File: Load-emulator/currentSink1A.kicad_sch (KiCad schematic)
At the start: 3 parts, among them Q2 TIP41C, U2 AD8001AN

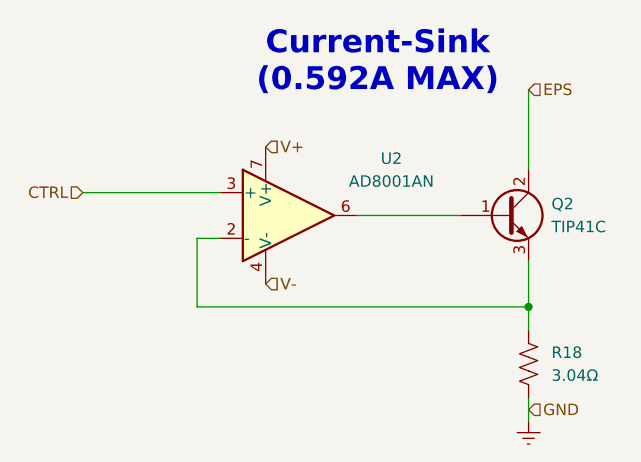
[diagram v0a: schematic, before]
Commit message: Replacement of the microcontroller w/ picoblade
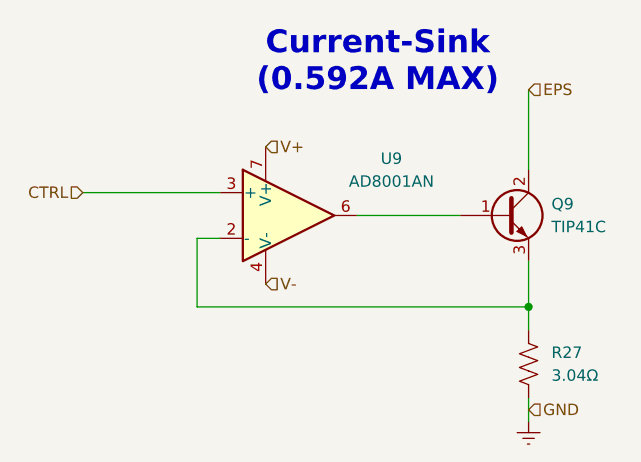
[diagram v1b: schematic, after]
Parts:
- renumbered Q2 to Q9, R18 to R27, U2 to U9
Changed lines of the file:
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@@
 		(dnp no)
 		(fields_autoplaced yes)
-		(property "Reference" "#PWR025"
+		(property "Reference" "#PWR060"
 			(at 162.56 114.3 0)
 			(effects
@@
 		(dnp no)
 		(fields_autoplaced yes)
-		(property "Reference" "Q2"
+		(property "Reference" "Q9"
 			(at 165.1 83.8199 0)
 			(effects
@@
 		(dnp no)
 		(fields_autoplaced yes)
-		(property "Reference" "U2"
+		(property "Reference" "U9"
 			(at 147.32 78.7714 0)
 			(effects
@@
 		(dnp no)
 		(fields_autoplaced yes)
-		(property "Reference" "R18"
+		(property "Reference" "R27"
 			(at 165.1 100.3299 0)
 			(effects

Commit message: Added footprints for the remaining resistors, capacitors and ampops, as well as some 3D models
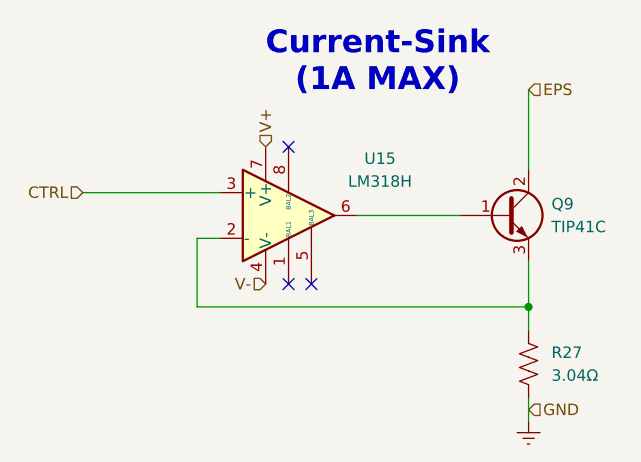
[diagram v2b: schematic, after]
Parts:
- removed U9: AD8001AN, Package_DIP:DIP-8_W7.62mm, symbol Amplifier_Operational:AD8001AN
- added U15: LM318H, symbol Amplifier_Operational:LM318H
- R27: footprint (none) -> Resistor_SMD:R_0201_0603Metric
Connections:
- net CTRL: now also U15.3 (+)
- net V+: now also U15.7 (V+)
- net V-: now also U15.4 (V-)
- net at Q9.1 (B): now also U15.6
- net at Q9.3 (E), R27.1: now also U15.2 (-)
- no-connect marks 0 -> 3
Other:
- note added: "Current-Sink (1A MAX)"
- note removed: "Current-Sink (0.592A MAX)"
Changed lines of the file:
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@@
 		(color 0 0 0 0)
 	)
+	(no_connect
+		(at 138.43 92.71)
+	)
+	(no_connect
+		(at 135.89 92.71)
+	)
+	(no_connect
+		(at 135.89 77.47)
+	)
 	(wire
 		(pts
@@
 		)
 	)
-	(text "Current-Sink\n(0.592A MAX)\n"
+	(text "Current-Sink\n(1A MAX)\n"
 		(exclude_from_sim no)
 		(at 145.796 68.072 0)
@@
 	(hierarchical_label "V-"
 		(shape input)
-		(at 133.35 92.71 0)
+		(at 133.35 92.71 180)
 		(fields_autoplaced yes)
 		(effects
@@
 				(size 1.27 1.27)
 			)
-			(justify left)
+			(justify right)
 		)
 	)
 	(hierarchical_label "V+"
 		(shape input)
-		(at 133.35 77.47 0)
+		(at 133.35 77.47 90)
 		(fields_autoplaced yes)
 		(effects
@@
 	)
 	(symbol
+		(lib_id "Amplifier_Operational:LM318H")
+		(at 135.89 85.09 0)
+		(unit 1)
+		(exclude_from_sim no)
+		(in_bom yes)
+		(on_board yes)
+		(dnp no)
+		(fields_autoplaced yes)
+		(property "Reference" "U15"
+			(at 146.05 78.7714 0)
+			(effects
+				(font
+					(size 1.27 1.27)
+				)
+			)
+		)
+		(property "Value" "LM318H"
+			(at 146.05 81.3114 0)
+			(effects
+				(font
+					(size 1.27 1.27)
+				)
+			)
+		)
+		(property "Footprint" ""
+			(at 135.89 85.09 0)
+			(effects
+				(font
+					(size 1.27 1.27)
+				)
+				(hide yes)
+			)
+		)
+		(property "Datasheet" "http://www.ti.com/lit/ds/symlink/lm318-n.pdf"
+			(at 135.89 85.09 0)
+			(effects
+				(font
+					(size 1.27 1.27)
+				)
+				(hide yes)
+			)
+		)
+		(property "Description" "Operational Amplifier, TO-99-8"
+			(at 135.89 85.09 0)
+			(effects
+				(font
+					(size 1.27 1.27)
+				)
+				(hide yes)
+			)
+		)
+		(pin "6"
+		)
+		(pin "5"
+		)
+		(pin "1"
+		)
+		(pin "4"
+		)
+		(pin "3"
+		)
+		(pin "2"
+		)
+		(pin "8"
+		)
+		(pin "7"
+		)
+		(instances
+			(project ""
+				(path "/9054bfd2-3cc0-4c96-aa71-abdb09b76dc7/a12c045f-372a-4c5b-93d1-0c234b5f9c5c/00308429-beaf-4782-9e5d-10502f61f5c3"
+					(reference "U17")
+					(unit 1)
+				)
+				(path "/9054bfd2-3cc0-4c96-aa71-abdb09b76dc7/a12c045f-372a-4c5b-93d1-0c234b5f9c5c/1067bc1d-731b-4056-a052-e9f9516161f7"
+					(reference "U15")
+					(unit 1)
+				)
+				(path "/9054bfd2-3cc0-4c96-aa71-abdb09b76dc7/a12c045f-372a-4c5b-93d1-0c234b5f9c5c/205d1fd4-c06c-4b81-92b9-38f15798e8a4"
+					(reference "U14")
+					(unit 1)
+				)
+				(path "/9054bfd2-3cc0-4c96-aa71-abdb09b76dc7/a12c045f-372a-4c5b-93d1-0c234b5f9c5c/7c366463-52c3-40cf-bddf-8ecdc0d5aa81"
+					(reference "U18")
+					(unit 1)
+				)
+				(path "/9054bfd2-3cc0-4c96-aa71-abdb09b76dc7/a12c045f-372a-4c5b-93d1-0c234b5f9c5c/9489fc74-437b-459f-aea1-db601c07bed5"
+					(reference "U16")
+					(unit 1)
+				)
+			)
+		)
+	)
+	(symbol
 		(lib_id "Transistor_BJT:TIP41C")
 		(at 160.02 85.09 0)
@@
 				(path "/9054bfd2-3cc0-4c96-aa71-abdb09b76dc7/a12c045f-372a-4c5b-93d1-0c234b5f9c5c/9489fc74-437b-459f-aea1-db601c07bed5"
 					(reference "Q6")
-					(unit 1)
-				)
-			)
-		)
-	)
-	(symbol
-		(lib_id "Amplifier_Operational:AD8001AN")
-		(at 135.89 85.09 0)
-		(unit 1)
-		(exclude_from_sim no)
-		(in_bom yes)
-		(on_board yes)
-		(dnp no)
-		(fields_autoplaced yes)
-		(property "Reference" "U9"
-			(at 147.32 78.7714 0)
-			(effects
-				(font
-					(size 1.27 1.27)
-				)
-			)
-		)
-		(property "Value" "AD8001AN"
-			(at 147.32 81.3114 0)
-			(effects
-				(font
-					(size 1.27 1.27)
-				)
-			)
-		)
-		(property "Footprint" "Package_DIP:DIP-8_W7.62mm"
-			(at 133.35 90.17 0)
-			(effects
-				(font
-					(size 1.27 1.27)
-				)
-				(justify left)
-				(hide yes)
-			)
-		)
-		(property "Datasheet" "https://www.analog.com/media/en/technical-documentation/data-sheets/ad8001.pdf"
-			(at 139.7 81.28 0)
-			(effects
-				(font
-					(size 1.27 1.27)
-				)
-				(hide yes)
-			)
-		)
-		(property "Description" "Current Feedback Amplifier, 800 MHz, 50mW, DIP-8"
-			(at 135.89 85.09 0)
-			(effects
-				(font
-					(size 1.27 1.27)
-				)
-				(hide yes)
-			)
-		)
-		(pin "6"
-		)
-		(pin "1"
-		)
-		(pin "3"
-		)
-		(pin "8"
-		)
-		(pin "5"
-		)
-		(pin "4"
-		)
-		(pin "7"
-		)
-		(pin "2"
-		)
-		(instances
-			(project "Load-emulator"
-				(path "/9054bfd2-3cc0-4c96-aa71-abdb09b76dc7/a12c045f-372a-4c5b-93d1-0c234b5f9c5c/00308429-beaf-4782-9e5d-10502f61f5c3"
-					(reference "U9")
-					(unit 1)
-				)
-				(path "/9054bfd2-3cc0-4c96-aa71-abdb09b76dc7/a12c045f-372a-4c5b-93d1-0c234b5f9c5c/1067bc1d-731b-4056-a052-e9f9516161f7"
-					(reference "U3")
-					(unit 1)
-				)
-				(path "/9054bfd2-3cc0-4c96-aa71-abdb09b76dc7/a12c045f-372a-4c5b-93d1-0c234b5f9c5c/205d1fd4-c06c-4b81-92b9-38f15798e8a4"
-					(reference "U2")
-					(unit 1)
-				)
-				(path "/9054bfd2-3cc0-4c96-aa71-abdb09b76dc7/a12c045f-372a-4c5b-93d1-0c234b5f9c5c/7c366463-52c3-40cf-bddf-8ecdc0d5aa81"
-					(reference "U12")
-					(unit 1)
-				)
-				(path "/9054bfd2-3cc0-4c96-aa71-abdb09b76dc7/a12c045f-372a-4c5b-93d1-0c234b5f9c5c/9489fc74-437b-459f-aea1-db601c07bed5"
-					(reference "U6")
 					(unit 1)
 				)
@@
 			)
 		)
-		(property "Footprint" ""
+		(property "Footprint" "Resistor_SMD:R_0201_0603Metric"
 			(at 163.576 101.854 90)
 			(effects

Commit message: Forgot to save files before last commit
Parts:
- U15: footprint (none) -> LM318M:SOIC127P599X175-8N
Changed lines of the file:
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@@
 			)
 		)
-		(property "Footprint" ""
+		(property "Footprint" "LM318M:SOIC127P599X175-8N"
 			(at 135.89 85.09 0)
 			(effects

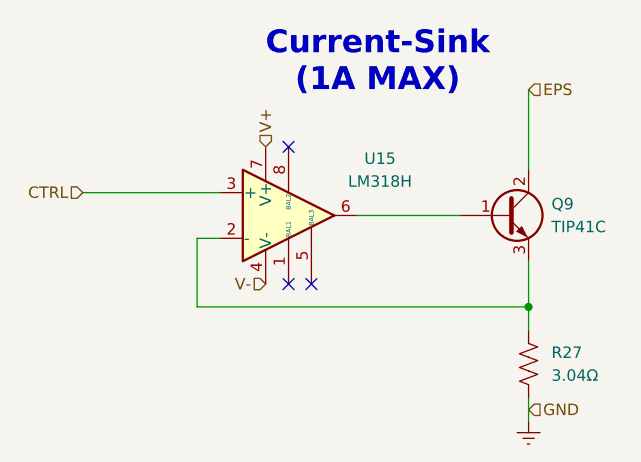
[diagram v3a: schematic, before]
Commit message: File with 3D models were created, because the models were previously saved at a local PC, so only one specific machine could load them; Better organization; EPS terminal labels were added to each current sink channel; Channels were searched for possible errors
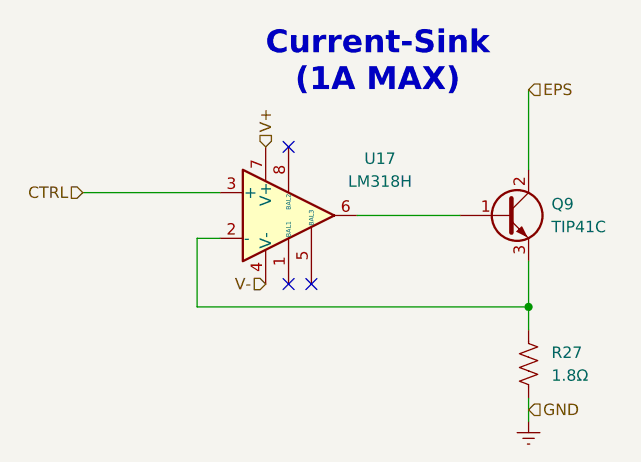
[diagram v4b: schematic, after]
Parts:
- R27: value 3.04Ω -> 1.8Ω
- renumbered U15 to U17
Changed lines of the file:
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@@
 		(dnp no)
 		(fields_autoplaced yes)
-		(property "Reference" "U15"
+		(property "Reference" "U17"
 			(at 146.05 78.7714 0)
 			(effects
@@
 			)
 		)
-		(property "Value" "3.04Ω"
+		(property "Value" "1.8Ω"
 			(at 165.1 102.8699 0)
 			(effects

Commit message: minor changes in connectors
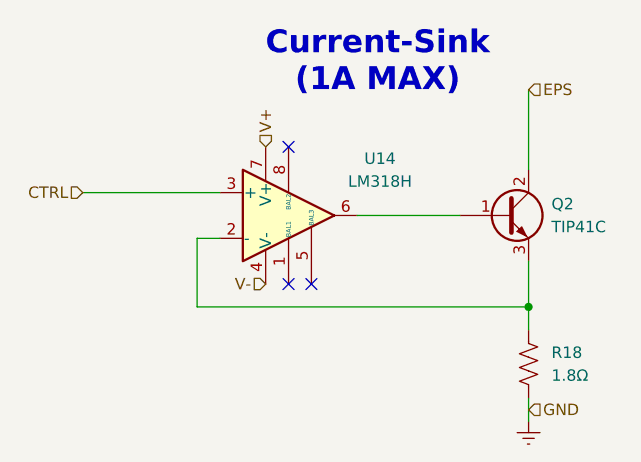
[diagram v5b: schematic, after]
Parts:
- renumbered Q9 to Q2, R27 to R18, U17 to U14
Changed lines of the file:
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@@
 (kicad_sch
-	(version 20231120)
+	(version 20250114)
 	(generator "eeschema")
-	(generator_version "8.0")
+	(generator_version "9.0")
 	(paper "A4")
+	(text "Current-Sink\n(1A MAX)\n"
+		(exclude_from_sim no)
+		(at 145.796 68.072 0)
+		(effects
+			(font
+				(size 2.54 2.54)
+				(thickness 0.254)
+				(bold yes)
+			)
+		)
+	)
 	(junction
 		(at 162.56 95.25)
@@
 		)
 	)
-	(text "Current-Sink\n(1A MAX)\n"
-		(exclude_from_sim no)
-		(at 145.796 68.072 0)
-		(effects
-			(font
-				(size 2.54 2.54)
-				(thickness 0.254)
-				(bold yes)
-			)
-		)
-	)
 	(hierarchical_label "CTRL"
 		(shape input)
 		(at 113.03 82.55 180)
-		(fields_autoplaced yes)
 		(effects
 			(font
@@
 		(shape input)
 		(at 162.56 106.68 0)
-		(fields_autoplaced yes)
 		(effects
 			(font
@@
 		(shape input)
 		(at 133.35 92.71 180)
-		(fields_autoplaced yes)
 		(effects
 			(font
@@
 		(shape input)
 		(at 133.35 77.47 90)
-		(fields_autoplaced yes)
 		(effects
 			(font
@@
 		(shape input)
 		(at 162.56 71.12 0)
-		(fields_autoplaced yes)
 		(effects
 			(font
@@
 		(dnp no)
 		(fields_autoplaced yes)
-		(property "Reference" "#PWR060"
+		(property "Reference" "#PWR025"
 			(at 162.56 114.3 0)
 			(effects
@@
 		(dnp no)
 		(fields_autoplaced yes)
-		(property "Reference" "U17"
+		(property "Reference" "U14"
 			(at 146.05 78.7714 0)
 			(effects
@@
 		(dnp no)
 		(fields_autoplaced yes)
-		(property "Reference" "Q9"
+		(property "Reference" "Q2"
 			(at 165.1 83.8199 0)
 			(effects
@@
 		(dnp no)
 		(fields_autoplaced yes)
-		(property "Reference" "R27"
+		(property "Reference" "R18"
 			(at 165.1 100.3299 0)
 			(effects
